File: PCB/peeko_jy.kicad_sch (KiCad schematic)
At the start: 6 parts, among them J1 Rasberry PI Pico, J2 Conn_02x15_Odd_Even, J3 Conn_01x02_Pin, J4 Conn_01x02_Pin

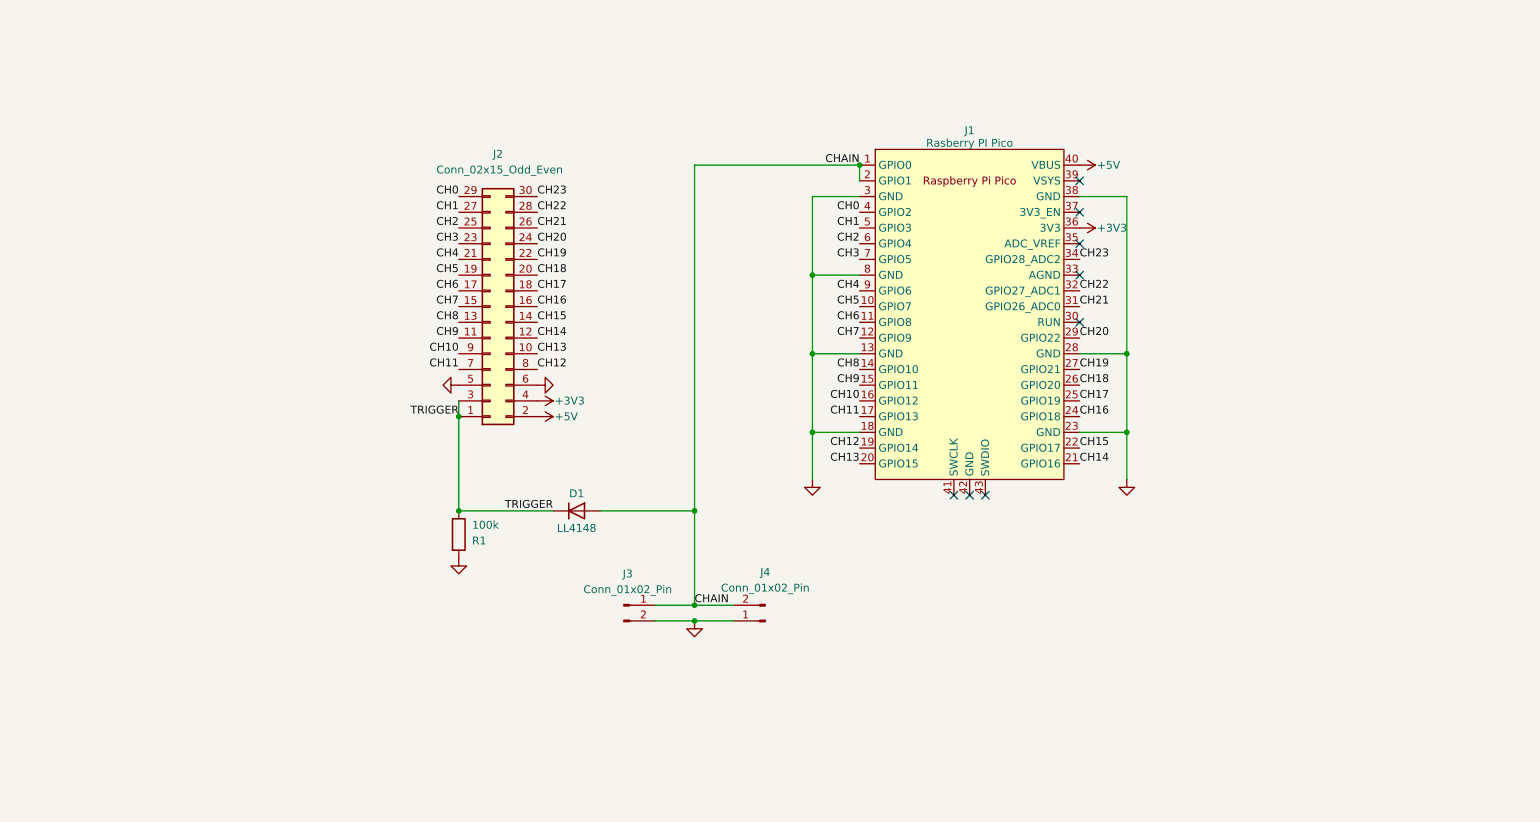
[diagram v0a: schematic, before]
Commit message: schematic for JY board, remove all but PCBs
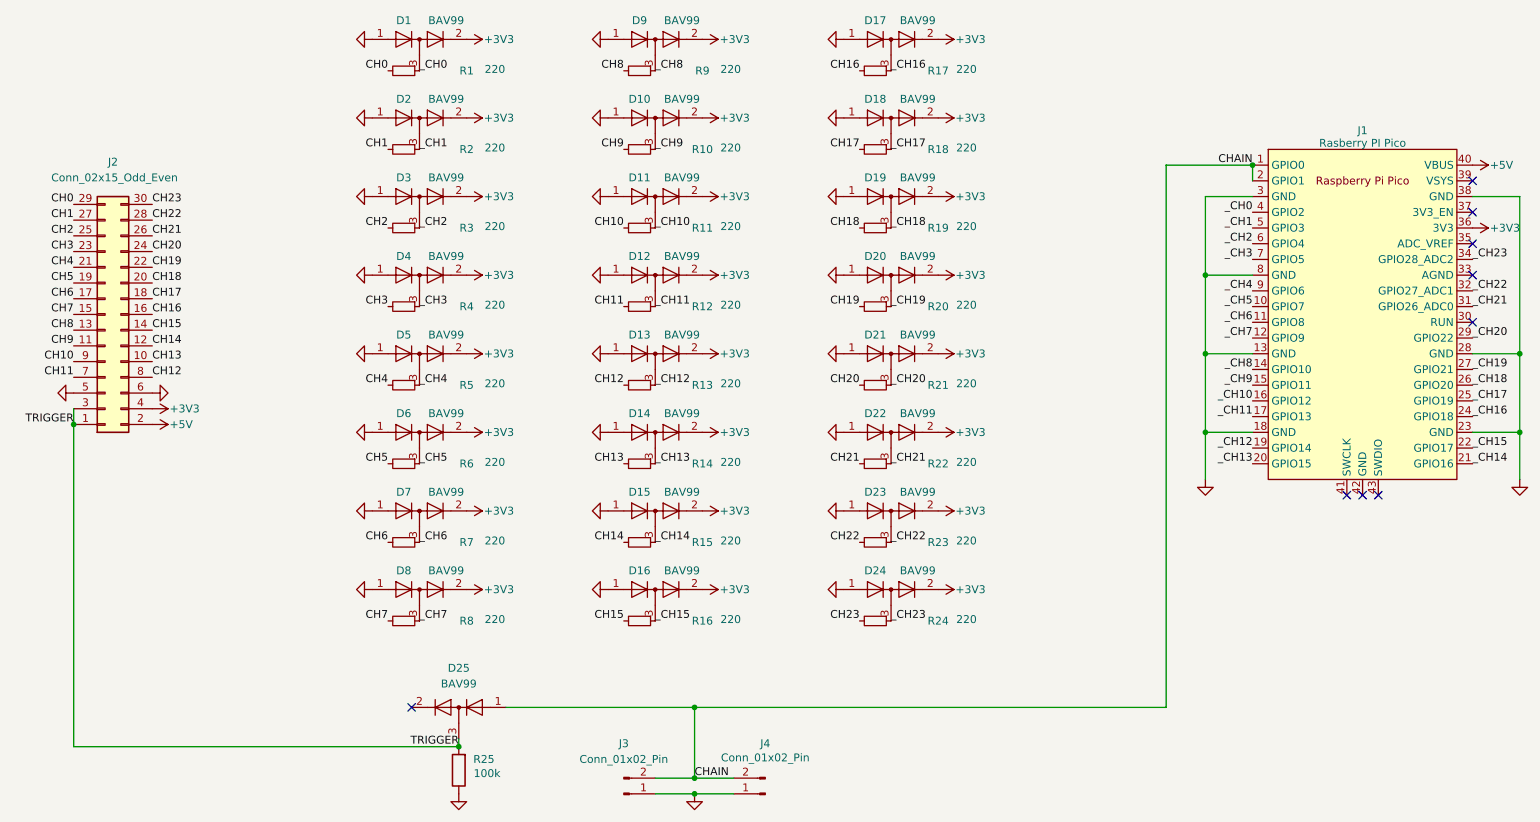
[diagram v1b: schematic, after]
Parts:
- removed D1: LL4148, 000_LOCAL:D_MiniMELF, symbol Diode:LL4148
- added D1, D10, D11, D12, D13, D14, D15, D16, D17, D18, D19, D2, D20, D21, D22, D23, D24, D25, D3, D4, D5, D6, D7, D8, D9: BAV99, 000_LOCAL:SC-59, symbol 000_LOCAL:BAV99
- added R1, R10, R11, R12, R13, R14, R15, R16, R17, R18, R19, R2, R20, R21, R22, R23, R24, R3, R4, R5, R6, R7, R8, R9: 220, 000_LOCAL:R_0805, symbol 000_LOCAL:R_Small
- J1: footprint 000_LOCAL:DIP_40_700 -> 000_LOCAL:dip-40-700-pi-pico
- J2: footprint Connector_IDC:IDC-Header_2x15_P2.54mm_Horizontal -> 000_LOCAL:IDC_02x15_2.54_THT_male_pcb_edge
- renumbered R1 to R25
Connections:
- net +3V3: now also D1.2 (A), D10.2 (A), D11.2 (A), D12.2 (A), D13.2 (A), D14.2 (A), D15.2 (A), D16.2 (A), D17.2 (A), D18.2 (A), D19.2 (A), D2.2 (A), D20.2 (A), D21.2 (A), D22.2 (A), D23.2 (A), D24.2 (A), D3.2 (A), D4.2 (A), D5.2 (A), D6.2 (A), D7.2 (A), D8.2 (A), D9.2 (A)
- net CH0: now also R1.2; no longer J1.4 (GPIO2)
- net CH1: now also R2.2; no longer J1.5 (GPIO3)
- net CH10: now also R11.2; no longer J1.16 (GPIO12)
- net CH11: now also R12.2; no longer J1.17 (GPIO13)
- net CH12: now also R13.2; no longer J1.19 (GPIO14)
- net CH13: now also R14.2; no longer J1.20 (GPIO15)
- net CH14: now also R15.2; no longer J1.21 (GPIO16)
- net CH15: now also R16.2; no longer J1.22 (GPIO17)
- net CH16: now also R17.2; no longer J1.24 (GPIO18)
- net CH17: now also R18.2; no longer J1.25 (GPIO19)
- net CH18: now also R19.2; no longer J1.26 (GPIO20)
- net CH19: now also R20.2; no longer J1.27 (GPIO21)
- net CH2: now also R3.2; no longer J1.6 (GPIO4)
- net CH20: now also R21.2; no longer J1.29 (GPIO22)
- net CH21: now also R22.2; no longer J1.31 (GPIO26_ADC0)
- net CH22: now also R23.2; no longer J1.32 (GPIO27_ADC1)
- net CH23: now also R24.2; no longer J1.34 (GPIO28_ADC2)
- net CH3: now also R4.2; no longer J1.7 (GPIO5)
- net CH4: now also R5.2; no longer J1.9 (GPIO6)
- net CH5: now also R6.2; no longer J1.10 (GPIO7)
- net CH6: now also R7.2; no longer J1.11 (GPIO8)
- net CH7: now also R8.2; no longer J1.12 (GPIO9)
- net CH8: now also R9.2; no longer J1.14 (GPIO10)
- net CH9: now also R10.2; no longer J1.15 (GPIO11)
- net CHAIN: now also J3.2 (Pin_2), D25.1 (K); no longer J3.1 (Pin_1)
- net GND: now also J3.1 (Pin_1), R25.1, D1.1 (K), D10.1 (K), D11.1 (K), D12.1 (K), D13.1 (K), D14.1 (K), D15.1 (K), D16.1 (K), D17.1 (K), D18.1 (K), D19.1 (K), D2.1 (K), D20.1 (K), D21.1 (K), D22.1 (K), D23.1 (K), D24.1 (K), D3.1 (K), D4.1 (K), D5.1 (K), D6.1 (K), D7.1 (K), D8.1 (K), D9.1 (K); no longer J3.2 (Pin_2), R25.2
- net TRIGGER: now also R25.2, D25.3 (K); no longer R25.1
- new net _CH0: D1.3 (K), J1.4 (GPIO2), R1.1
- new net _CH1: D2.3 (K), J1.5 (GPIO3), R2.1
- new net _CH10: D11.3 (K), J1.16 (GPIO12), R11.1
- new net _CH11: D12.3 (K), J1.17 (GPIO13), R12.1
- new net _CH12: D13.3 (K), J1.19 (GPIO14), R13.1
- new net _CH13: D14.3 (K), J1.20 (GPIO15), R14.1
- new net _CH14: D15.3 (K), J1.21 (GPIO16), R15.1
- new net _CH15: D16.3 (K), J1.22 (GPIO17), R16.1
- new net _CH16: D17.3 (K), J1.24 (GPIO18), R17.1
- new net _CH17: D18.3 (K), J1.25 (GPIO19), R18.1
- new net _CH18: D19.3 (K), J1.26 (GPIO20), R19.1
- new net _CH19: D20.3 (K), J1.27 (GPIO21), R20.1
- new net _CH2: D3.3 (K), J1.6 (GPIO4), R3.1
- new net _CH20: D21.3 (K), J1.29 (GPIO22), R21.1
- new net _CH21: D22.3 (K), J1.31 (GPIO26_ADC0), R22.1
- new net _CH22: D23.3 (K), J1.32 (GPIO27_ADC1), R23.1
- new net _CH23: D24.3 (K), J1.34 (GPIO28_ADC2), R24.1
- new net _CH3: D4.3 (K), J1.7 (GPIO5), R4.1
- new net _CH4: D5.3 (K), J1.9 (GPIO6), R5.1
- new net _CH5: D6.3 (K), J1.10 (GPIO7), R6.1
- new net _CH6: D7.3 (K), J1.11 (GPIO8), R7.1
- new net _CH7: D8.3 (K), J1.12 (GPIO9), R8.1
- new net _CH8: D9.3 (K), J1.14 (GPIO10), R9.1
- new net _CH9: D10.3 (K), J1.15 (GPIO11), R10.1
- no-connect marks 8 -> 9
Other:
- moved on the sheet: J1, J2, J3, J4, R25
